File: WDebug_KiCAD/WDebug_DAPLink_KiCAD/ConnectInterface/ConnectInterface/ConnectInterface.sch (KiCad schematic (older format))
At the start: 5 parts, among them J1 ConnDebug, J2 YOUGU_Debug

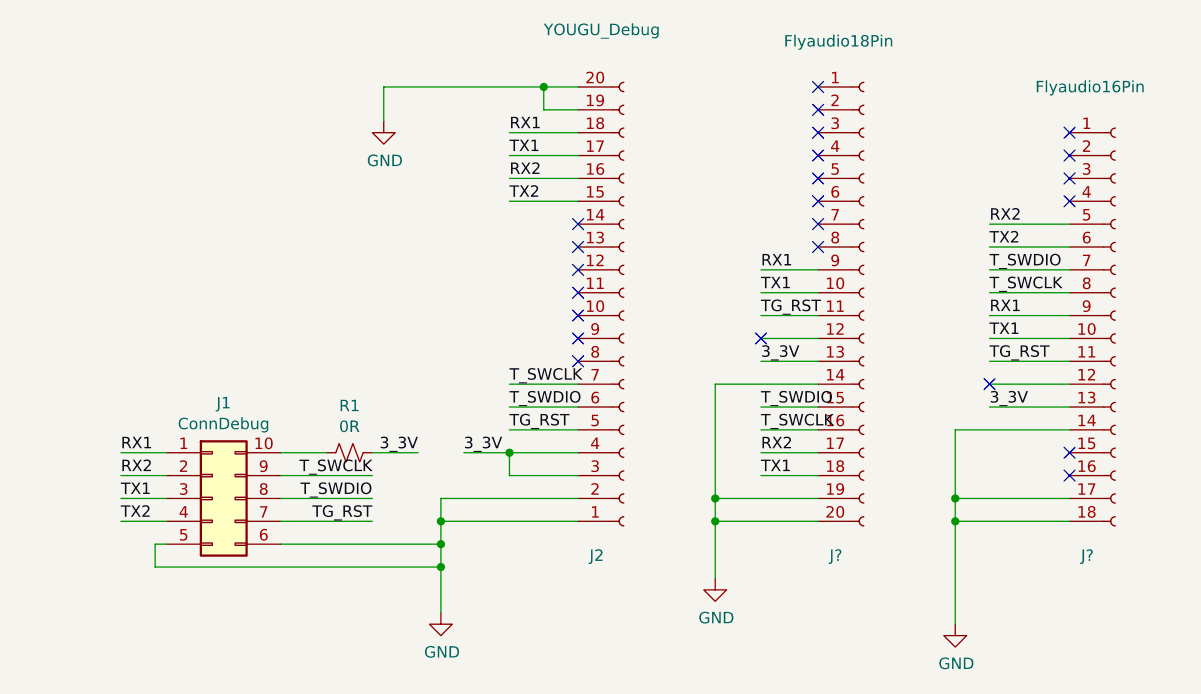
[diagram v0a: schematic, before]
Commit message: 修改转接板接口定义
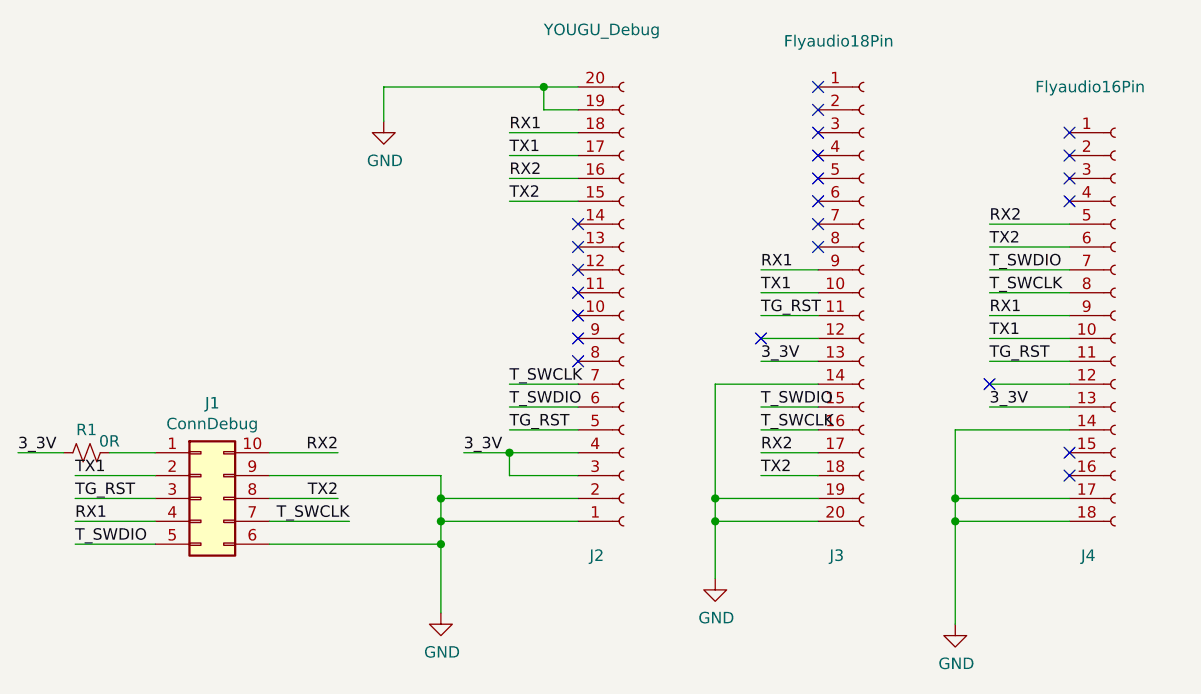
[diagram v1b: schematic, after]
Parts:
- J2: footprint WDebug_DAPLink:1x18_P1.0mm -> Connector_PinHeader_1.00mm:1x18_P1.0mm
- J3: renamed from J?; footprint WDebug_DAPLink:1x18_P1.0mm -> Connector_PinHeader_1.00mm:1x18_P1.0mm
- J4: renamed from J?; footprint (none) -> Connector_PinHeader_1.00mm:1x16_P1.0mm
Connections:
- net GND: now also J1.9 (Pin_9); no longer J1.5 (Pin_5)
- net RX1: now also J1.4 (Pin_4); no longer J1.1 (Pin_1)
- net RX2: now also J1.10 (Pin_10); no longer J1.2 (Pin_2)
- net TG_RST: now also J1.3 (Pin_3); no longer J1.7 (Pin_7)
- net TX1: now also J1.2 (Pin_2); no longer J1.3 (Pin_3), J3.18 (Pin_18)
- net TX2: now also J1.8 (Pin_8), J3.18 (Pin_18); no longer J1.4 (Pin_4)
- net T_SWCLK: now also J1.7 (Pin_7); no longer J1.9 (Pin_9)
- net T_SWDIO: now also J1.5 (Pin_5); no longer J1.8 (Pin_8)
- net at R1.2: now also J1.1 (Pin_1); no longer J1.10 (Pin_10)
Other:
- moved on the sheet: J1, R1
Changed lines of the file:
@@
 F 0 "J2" H 6250 4150 50  0000 L CNN
 F 1 "YOUGU_Debug" H 6050 1850 50  0000 L CNN
-F 2 "WDebug_DAPLink:1x18_P1.0mm" H 6400 3100 50  0001 C CNN
+F 2 "Connector_PinHeader_1.00mm:1x18_P1.0mm" H 6400 3100 50  0001 C CNN
 F 3 "" H 6400 3100 50  0001 C CNN
 	1    6400 3100
 	1    0    0    1
-$EndComp
-$Comp
-L Connector_Generic:Conn_02x05_Counter_Clockwise J1
-U 1 1 6161205F
-P 4600 3900
-F 0 "J1" H 4650 4317 50  0000 C CNN
-F 1 "ConnDebug" H 4650 4226 50  0000 C CNN
-F 2 "Connector_PinHeader_2.54mm:PinHeader_2x05_P2.54mm_Vertical" H 4600 3900 50  0001 C CNN
-F 3 "~" H 4600 3900 50  0001 C CNN
-	1    4600 3900
-	1    0    0    -1
 $EndComp
 $Comp
@@
 Wire Wire Line
 	6200 3400 5900 3400
-Wire Wire Line
-	4400 4100 4350 4100
-Wire Wire Line
-	4350 4100 4350 4200
-Wire Wire Line
-	4900 4100 5600 4100
-Wire Wire Line
-	4900 3800 5300 3800
-Wire Wire Line
-	4900 3900 5300 3900
-Wire Wire Line
-	4900 4000 5300 4000
-Text Label 5300 3800 2    50   ~ 0
+Text Label 5200 4000 2    50   ~ 0
 T_SWCLK
-Text Label 5300 3900 2    50   ~ 0
+Text Label 4000 4100 0    50   ~ 0
 T_SWDIO
-Text Label 5300 4000 2    50   ~ 0
+Text Label 4000 3900 0    50   ~ 0
 TG_RST
 Wire Wire Line
-	4400 3700 4200 3700
-Wire Wire Line
-	4400 3800 4200 3800
-Wire Wire Line
-	4400 3900 4200 3900
-Wire Wire Line
-	4400 4000 4200 4000
-Text Label 4200 3700 0    50   ~ 0
+	4350 4000 4000 4000
+Wire Wire Line
+	4350 3800 4000 3800
+Text Label 4000 4000 0    50   ~ 0
 RX1
-Text Label 4200 3800 0    50   ~ 0
+Text Label 5150 3700 2    50   ~ 0
 RX2
-Text Label 4200 3900 0    50   ~ 0
+Text Label 4000 3800 0    50   ~ 0
 TX1
-Text Label 4200 4000 0    50   ~ 0
-TX2
 Text Label 5900 3600 0    50   ~ 0
 TG_RST
@@
 	6200 2300 5900 2300
 Connection ~ 5600 4100
-Wire Wire Line
-	4350 4200 5600 4200
-Wire Wire Line
-	5600 4100 5600 4200
-Connection ~ 5600 4200
-Wire Wire Line
-	5600 4200 5600 4400
 NoConn ~ 6200 3200
 NoConn ~ 6200 3300
@@
 Connection ~ 6050 2100
 $Comp
-L WDebug_KiCAD-rescue:Conn_01x20_Female-Connector J?
+L WDebug_KiCAD-rescue:Conn_01x20_Female-Connector J3
 U 1 1 61DDBAC2
 P 7450 3000
-F 0 "J?" H 7300 1850 50  0000 L CNN
+F 0 "J3" H 7300 1850 50  0000 L CNN
 F 1 "Flyaudio18Pin" H 7100 4100 50  0000 L CNN
-F 2 "WDebug_DAPLink:1x18_P1.0mm" H 7450 3000 50  0001 C CNN
+F 2 "Connector_PinHeader_1.00mm:1x18_P1.0mm" H 7450 3000 50  0001 C CNN
 F 3 "" H 7450 3000 50  0001 C CNN
 	1    7450 3000
@@
 $EndComp
 $Comp
-L Connector:Conn_01x18_Female J?
+L Connector:Conn_01x18_Female J4
 U 1 1 61DE2FE0
 P 8550 3100
-F 0 "J?" H 8400 2050 50  0000 L CNN
+F 0 "J4" H 8400 2050 50  0000 L CNN
 F 1 "Flyaudio16Pin" H 8200 4100 50  0000 L CNN
-F 2 "" H 8550 3100 50  0001 C CNN
+F 2 "Connector_PinHeader_1.00mm:1x16_P1.0mm" H 8550 3100 50  0001 C CNN
 F 3 "~" H 8550 3100 50  0001 C CNN
 	1    8550 3100
@@
 $EndComp
 $Comp
-L power:GND #PWR?
+L power:GND #PWR0101
 U 1 1 61DE9B54
 P 6800 4250
-F 0 "#PWR?" H 6800 4000 50  0001 C CNN
+F 0 "#PWR0101" H 6800 4000 50  0001 C CNN
 F 1 "GND" H 6805 4077 50  0000 C CNN
 F 2 "" H 6800 4250 50  0001 C CNN
@@
 NoConn ~ 7250 2100
 $Comp
-L power:GND #PWR?
+L power:GND #PWR0104
 U 1 1 61DFFCCC
 P 7850 4450
-F 0 "#PWR?" H 7850 4200 50  0001 C CNN
+F 0 "#PWR0104" H 7850 4200 50  0001 C CNN
 F 1 "GND" H 7855 4277 50  0000 C CNN
 F 2 "" H 7850 4450 50  0001 C CNN
@@
 L Device:R_Small_US R1
 U 1 1 61619B46
-P 5200 3700
-F 0 "R1" V 4995 3700 50  0000 C CNN
-F 1 "0R" V 5086 3700 50  0000 C CNN
-F 2 "Resistor_SMD:R_0603_1608Metric" H 5200 3700 50  0001 C CNN
-F 3 "~" H 5200 3700 50  0001 C CNN
-	1    5200 3700
-	0    1    1    0
-$EndComp
-Wire Wire Line
-	4900 3700 5100 3700
-Wire Wire Line
-	5300 3700 5500 3700
+P 4050 3700
+F 0 "R1" V 4150 3700 50  0000 C CNN
+F 1 "0R" V 4100 3600 50  0000 C CNN
+F 2 "Resistor_SMD:R_0603_1608Metric" H 4050 3700 50  0001 C CNN
+F 3 "~" H 4050 3700 50  0001 C CNN
+	1    4050 3700
+	0    -1   -1   0
+$EndComp
+Wire Wire Line
+	4350 3700 4150 3700
+Wire Wire Line
+	3950 3700 3750 3700
 Wire Wire Line
 	5900 3700 5700 3700
 Connection ~ 5900 3700
-Text Label 5500 3700 2    50   ~ 0
+Text Label 3750 3700 0    50   ~ 0
 3_3V
 Text Label 5700 3700 0    50   ~ 0
@@
 RX2
 Text Label 7000 3800 0    50   ~ 0
-TX1
+TX2
 Text Label 8000 3500 0    50   ~ 0
 3_3V
@@
 NoConn ~ 8000 3400
 NoConn ~ 7000 3200
+Wire Wire Line
+	5600 4100 5600 4400
+Wire Wire Line
+	5600 3800 5600 3900
+Connection ~ 5600 3900
+Wire Wire Line
+	4850 3800 5600 3800
+Wire Wire Line
+	4850 4000 5200 4000
+Wire Wire Line
+	4850 4100 5600 4100
+Wire Wire Line
+	4000 4100 4350 4100
+Wire Wire Line
+	4350 3900 4000 3900
+Wire Wire Line
+	4850 3700 5150 3700
+$Comp
+L Connector_Generic:Conn_02x05_Counter_Clockwise J1
+U 1 1 6161205F
+P 4550 3900
+F 0 "J1" H 4600 4317 50  0000 C CNN
+F 1 "ConnDebug" H 4600 4226 50  0000 C CNN
+F 2 "Connector_PinHeader_2.54mm:PinHeader_2x05_P2.54mm_Vertical" H 4550 3900 50  0001 C CNN
+F 3 "~" H 4550 3900 50  0001 C CNN
+	1    4550 3900
+	1    0    0    -1
+$EndComp
+Wire Wire Line
+	4850 3900 5150 3900
+Text Label 5150 3900 2    50   ~ 0
+TX2
 $EndSCHEMATC
